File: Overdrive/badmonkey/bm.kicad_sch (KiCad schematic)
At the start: 37 parts, among them J1 Conn_01x04_Pin, Q1 2N3904, U1 4558, U2 4558

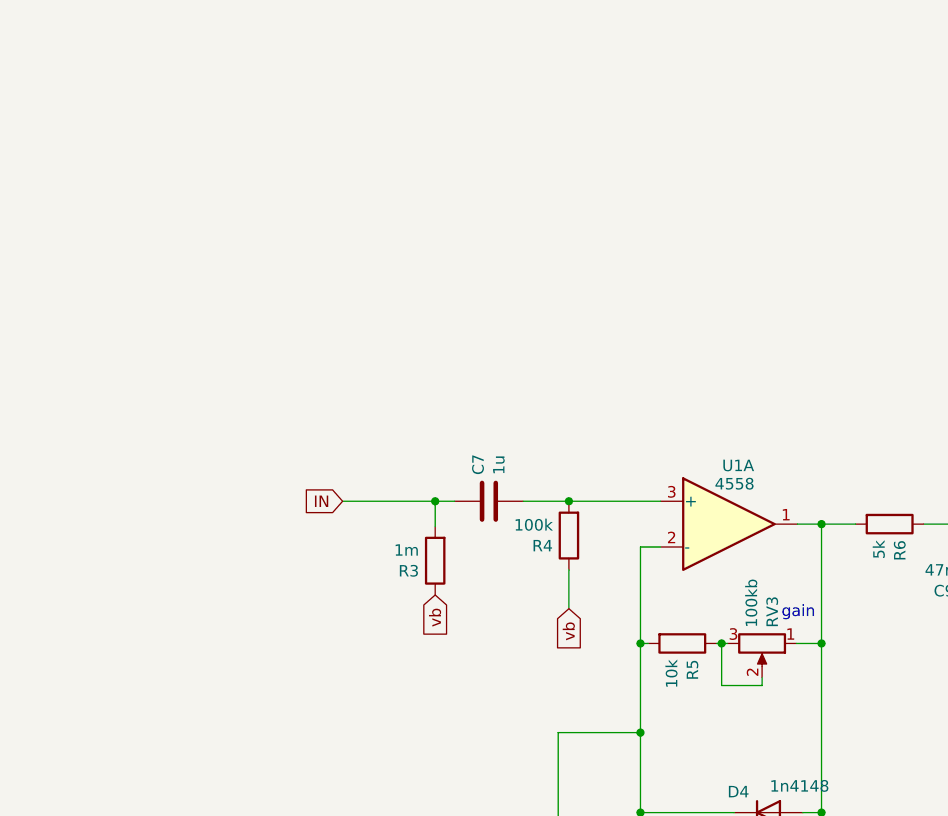
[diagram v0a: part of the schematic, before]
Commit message: fix to badmonkey -- pedal works but the schematic this was based on does not seem right.   There's a voltage offset on the input when engaged, and this messes with it in the pedal chain.
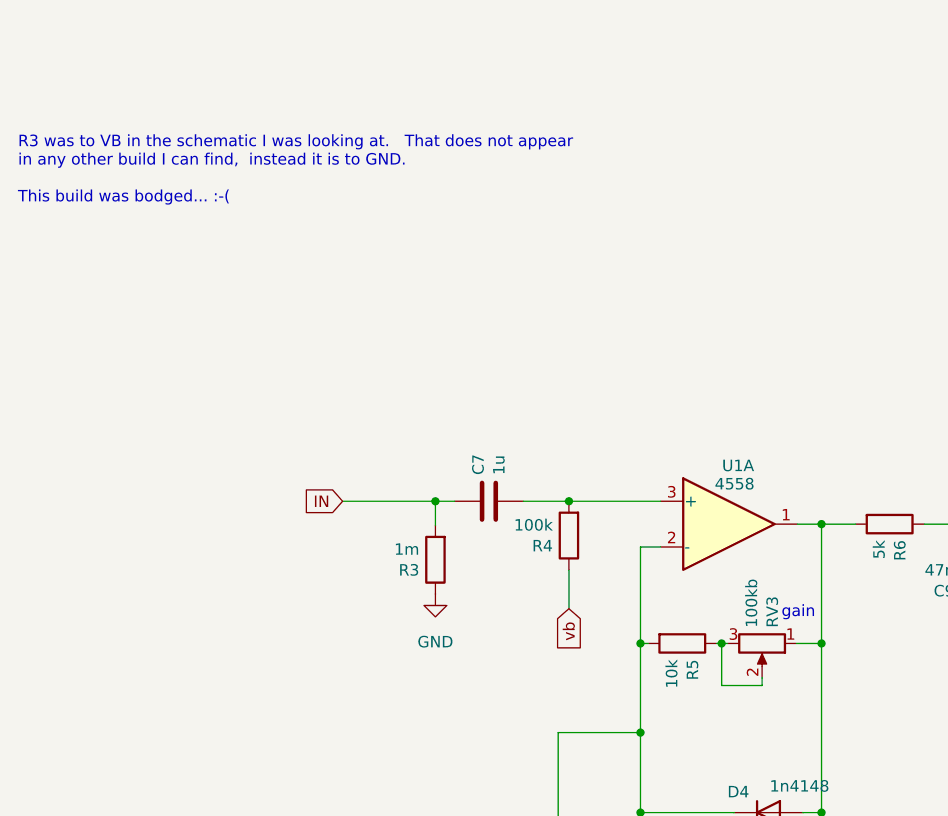
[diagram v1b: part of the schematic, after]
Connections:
- net GND: now also R3.1
- net vb: no longer R3.1
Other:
- note added: "R3 was to VB in the schematic I was looking at. That does not appear in any other build I can find, instead it is to GND. This build was bodged... :-("

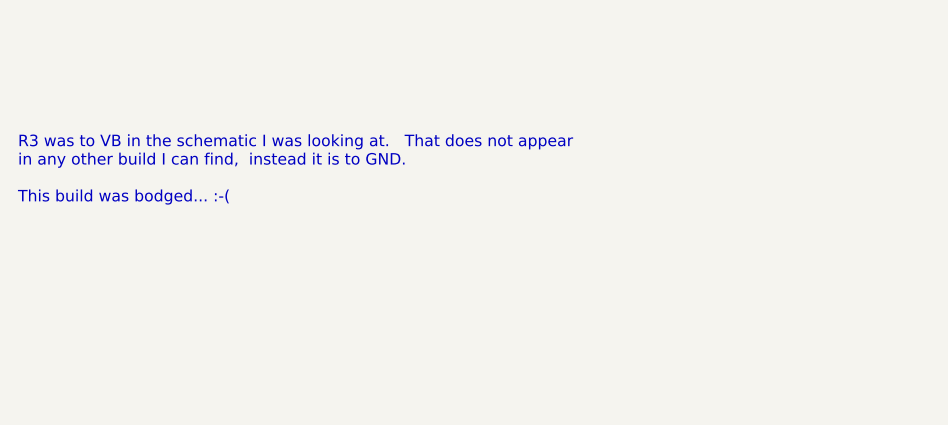
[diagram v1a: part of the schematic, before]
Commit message: added 6 band eq, and fuzzface distortion
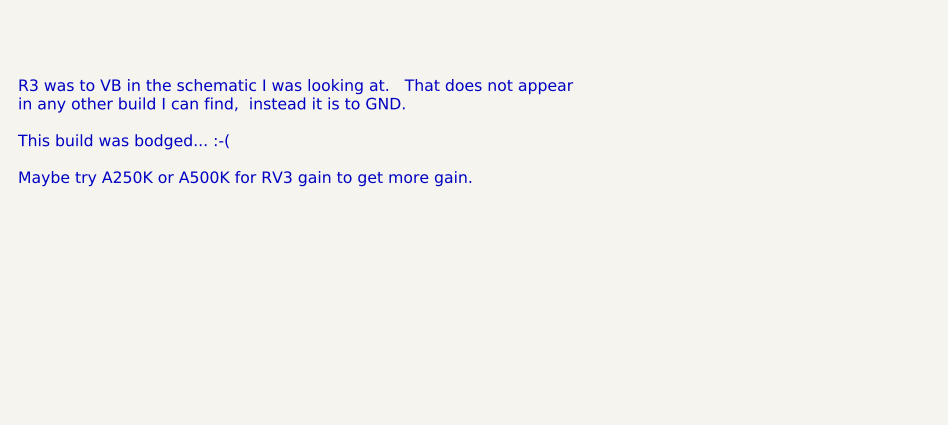
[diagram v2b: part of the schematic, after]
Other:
- note added: "R3 was to VB in the schematic I was looking at. That does not appear in any other build I can find, instead it is to GND. This build was bodged... :-( Maybe try A250K or A500K for RV3 gain to get more gain."
- note removed: "R3 was to VB in the schematic I was looking at. That does not appear in any other build I can find, instead it is to GND. This build was bodged... :-("
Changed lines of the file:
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@@
     (effects (font (size 1.27 1.27)) (justify left bottom))
   )
-  (text "R3 was to VB in the schematic I was looking at.   That does not appear\nin any other build I can find,  instead it is to GND.\n\nThis build was bodged... :-(\n"
+  (text "R3 was to VB in the schematic I was looking at.   That does not appear\nin any other build I can find,  instead it is to GND.\n\nThis build was bodged... :-(\n\nMaybe try A250K or A500K for RV3 gain to get more gain.\n\n"
     (at 22.6568 38.1508 0)
     (effects (font (size 1.27 1.27)) (justify left bottom))
